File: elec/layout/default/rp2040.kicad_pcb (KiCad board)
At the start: 2 copper layers, 20 parts, among them U1 RP2040, U2 _X322512MSB4SI, U3 _W25Q128JVSIQ

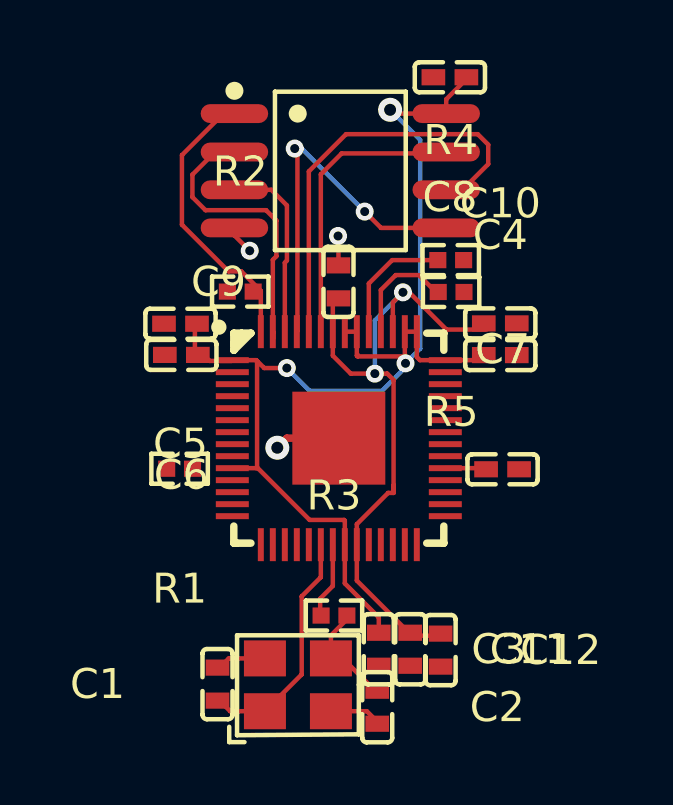
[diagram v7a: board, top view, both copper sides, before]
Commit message: Add new layout properties to PCB
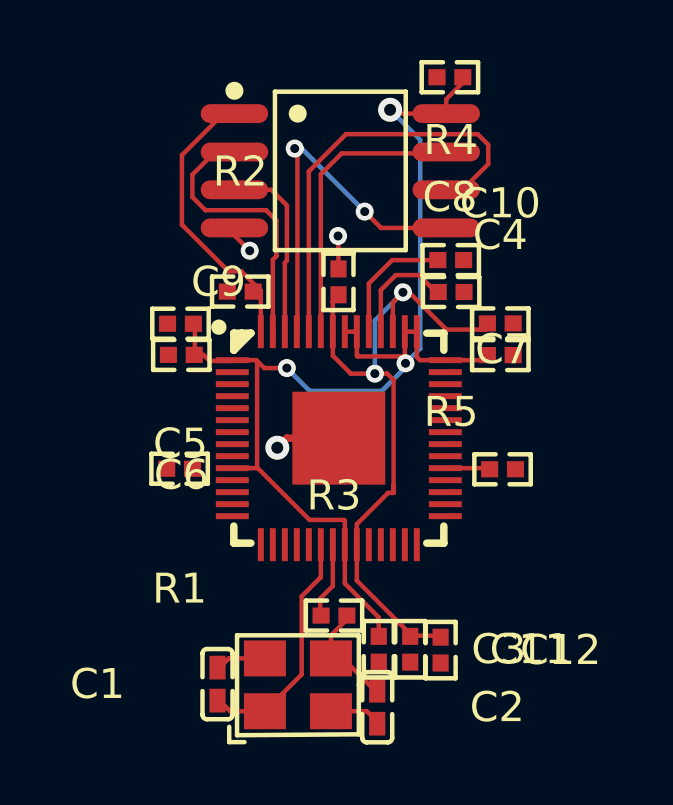
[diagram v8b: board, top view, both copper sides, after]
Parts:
- C1, C2: footprint lcsc:C0402 -> atopile:C0402-b3ef17
- C10, C11, C12, C3, C4, C5, C6, C7, C8, C9: footprint lcsc:C0402 -> lib:R0402
- R1, R2, R3, R4, R5: footprint lcsc:R0402 -> atopile:R0402-56259e
- U1: value RP2040 -> (none)
- U2: value _X322512MSB4SI -> (none)
- U3: value _W25Q128JVSIQ -> (none)
